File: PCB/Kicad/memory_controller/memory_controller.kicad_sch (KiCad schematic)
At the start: 4 parts

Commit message: fix
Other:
- removed sheet memory_tri_state_buffer
- sheet RegAddr ports: added ~{CLK_en}; removed nCLKen
- sheet input_MUX ports: added ~{OE}_n, ~{OE}_p; removed nOE_n, nOE_p
- sheet input_tri_state_buffer ports: added ~{OE}; removed nOE
- sheet memory_logic ports: added ~{OE}_MUX_n, ~{OE}_MUX_p, ~{WE}_mem; removed memory_logic_OUT, muxnOE_n, muxnOE_p, nWE_mem
- sheet mode_logic ports: added ~{OE}_n, ~{OE}_p, ~{OUTPUT_ENABLE}; removed nOE_n, nOE_p, nOUTPUT_ENABLE
- sheet output_MUX ports: added ~{OE}_n, ~{OE}_p; removed nOE_n, nOE_p
- sheet output_tri_state_buffer ports: added ~{OE}; removed nOE

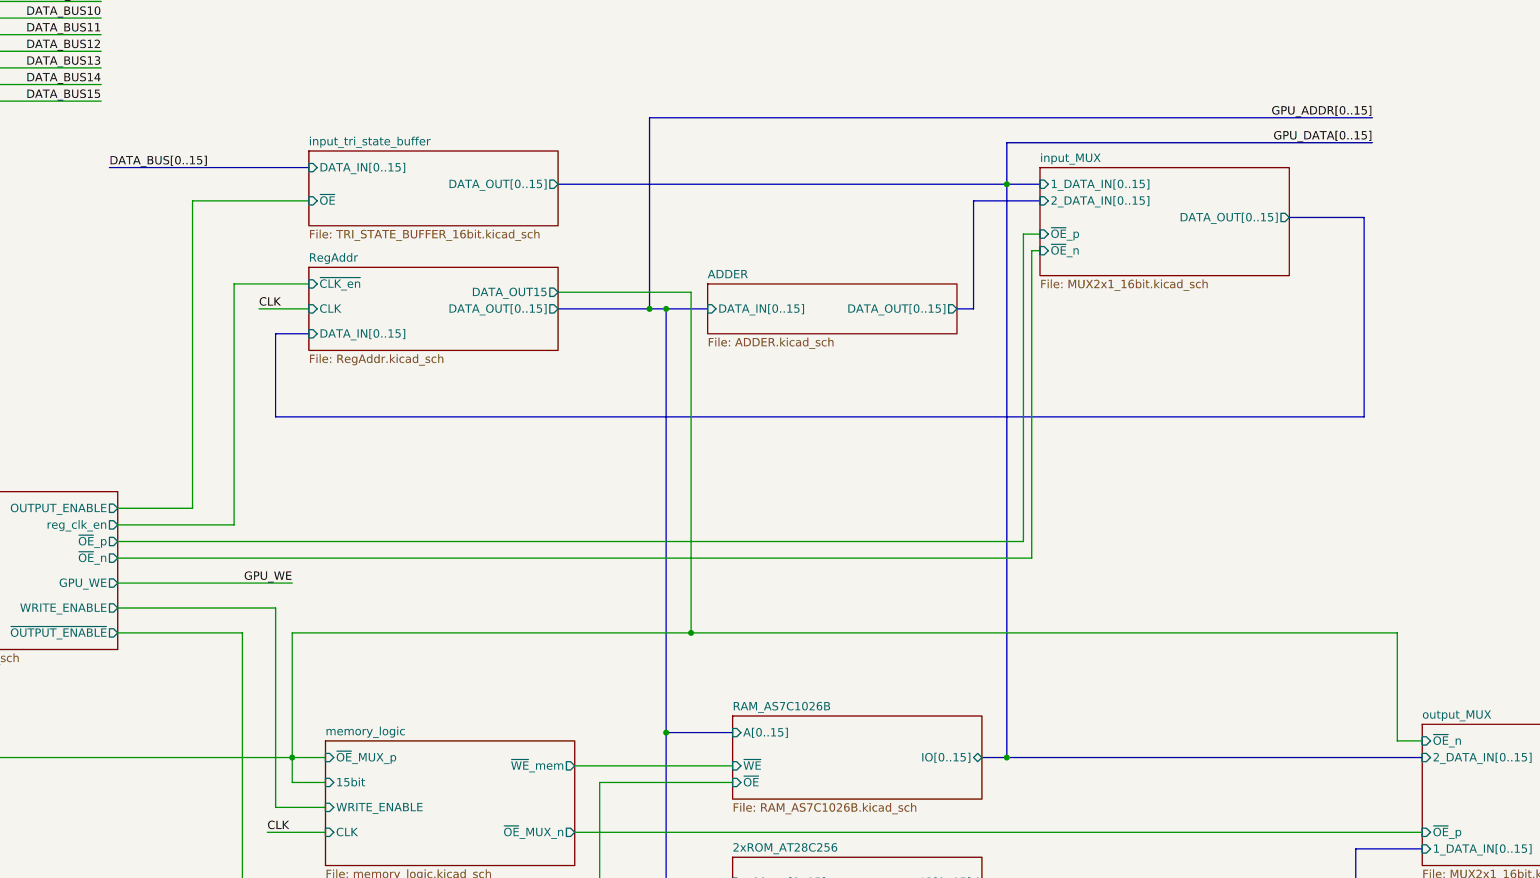
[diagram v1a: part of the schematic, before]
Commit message: memory controler fix
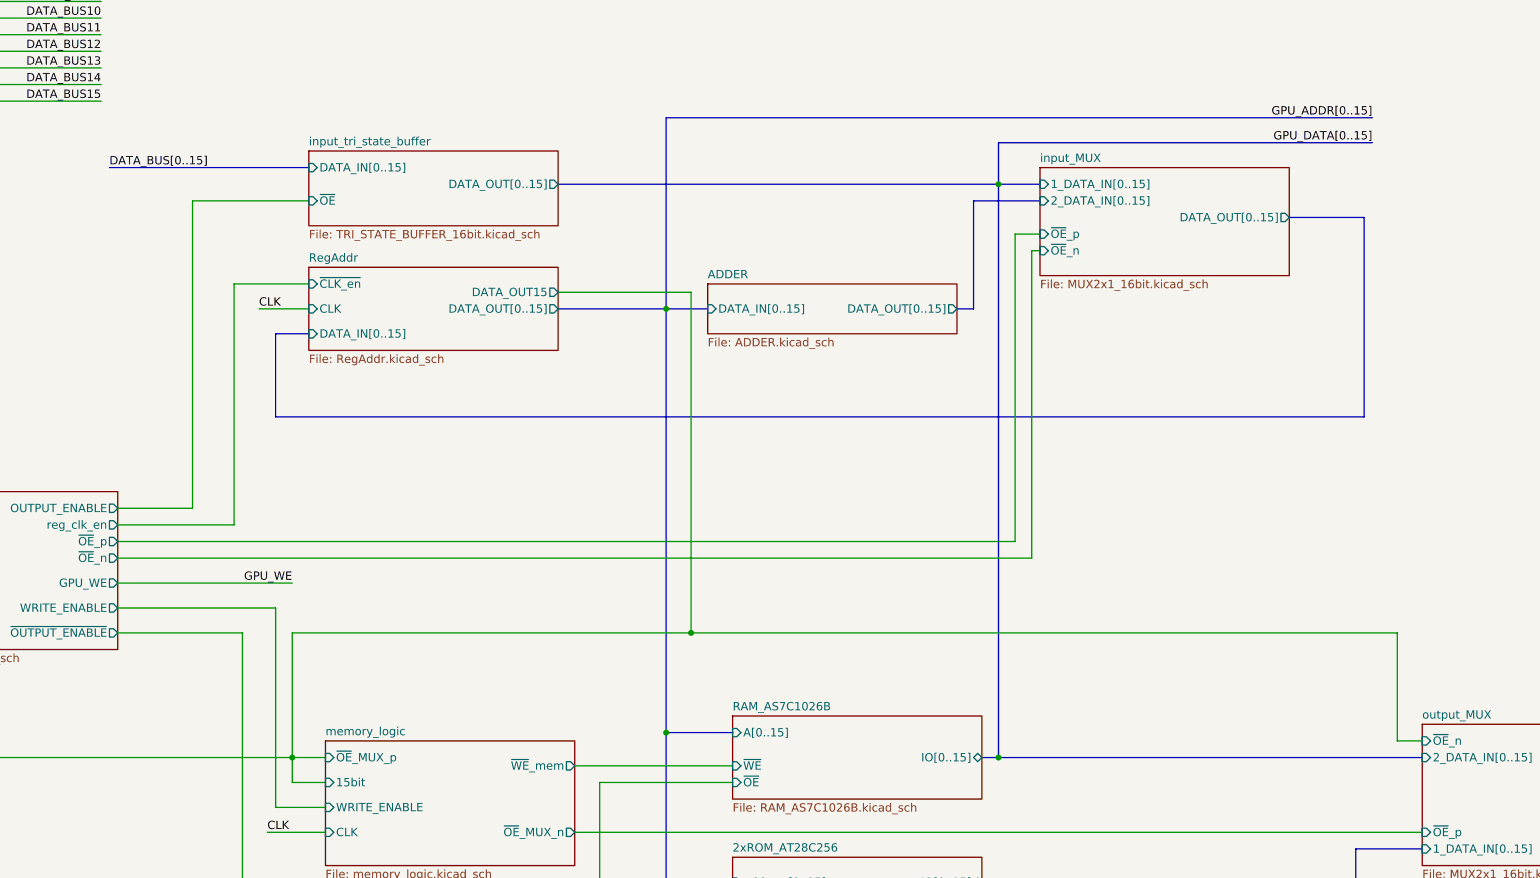
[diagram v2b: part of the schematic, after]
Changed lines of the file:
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@@
 	)
 	(junction
-		(at 227.33 191.77)
+		(at 226.06 191.77)
 		(diameter 0)
 		(color 0 0 0 0)
 	)
 	(junction
-		(at 227.33 104.14)
+		(at 226.06 104.14)
 		(diameter 0)
 		(color 0 0 0 0)
@@
 		(color 0 0 0 0)
 	)
-	(junction
-		(at 172.72 123.19)
-		(diameter 0)
-		(color 0 0 0 0)
-	)
 	(no_connect
 		(at 125.73 63.5)
@@
 	(bus
 		(pts
-			(xy 227.33 97.79) (xy 283.21 97.79)
+			(xy 226.06 97.79) (xy 283.21 97.79)
 		)
 		(stroke
@@
 	(bus
 		(pts
-			(xy 172.72 93.98) (xy 283.21 93.98)
+			(xy 175.26 93.98) (xy 283.21 93.98)
 		)
 		(stroke
@@
 	(bus
 		(pts
-			(xy 158.75 104.14) (xy 227.33 104.14)
+			(xy 158.75 104.14) (xy 226.06 104.14)
 		)
 		(stroke
@@
 	(bus
 		(pts
-			(xy 158.75 123.19) (xy 172.72 123.19)
+			(xy 158.75 123.19) (xy 175.26 123.19)
 		)
 		(stroke
@@
 	(bus
 		(pts
-			(xy 172.72 123.19) (xy 172.72 93.98)
+			(xy 175.26 123.19) (xy 175.26 93.98)
 		)
 		(stroke
@@
 		)
 	)
-	(bus
-		(pts
-			(xy 290.83 191.77) (xy 227.33 191.77)
-		)
-		(stroke
-			(width 0)
-			(type default)
-		)
-	)
 	(wire
 		(pts
@@
 	(wire
 		(pts
-			(xy 91.44 158.75) (xy 229.87 158.75)
+			(xy 91.44 158.75) (xy 228.6 158.75)
 		)
 		(stroke
@@
 	(wire
 		(pts
-			(xy 229.87 111.76) (xy 229.87 158.75)
+			(xy 228.6 111.76) (xy 228.6 158.75)
 		)
 		(stroke
@@
 	(bus
 		(pts
-			(xy 227.33 97.79) (xy 227.33 104.14)
+			(xy 226.06 97.79) (xy 226.06 104.14)
 		)
 		(stroke
@@
 		)
 	)
-	(bus
-		(pts
-			(xy 227.33 104.14) (xy 232.41 104.14)
-		)
-		(stroke
-			(width 0)
-			(type default)
-		)
-	)
 	(wire
 		(pts
@@
 		)
 	)
+	(bus
+		(pts
+			(xy 226.06 104.14) (xy 232.41 104.14)
+		)
+		(stroke
+			(width 0)
+			(type default)
+		)
+	)
 	(wire
 		(pts
@@
 		)
 	)
-	(bus
-		(pts
-			(xy 175.26 123.19) (xy 172.72 123.19)
-		)
-		(stroke
-			(width 0)
-			(type default)
-		)
-	)
 	(wire
 		(pts
@@
 	(bus
 		(pts
-			(xy 227.33 104.14) (xy 227.33 191.77)
+			(xy 226.06 104.14) (xy 226.06 191.77)
 		)
 		(stroke
@@
 	(wire
 		(pts
-			(xy 229.87 111.76) (xy 232.41 111.76)
+			(xy 228.6 111.76) (xy 232.41 111.76)
 		)
 		(stroke
@@
 		)
 	)
+	(bus
+		(pts
+			(xy 226.06 191.77) (xy 290.83 191.77)
+		)
+		(stroke
+			(width 0)
+			(type default)
+		)
+	)
 	(wire
 		(pts
@@
 	(bus
 		(pts
-			(xy 223.52 191.77) (xy 227.33 191.77)
-		)
-		(stroke
+			(xy 223.52 191.77) (xy 226.06 191.77)
+		)
+		(stroke

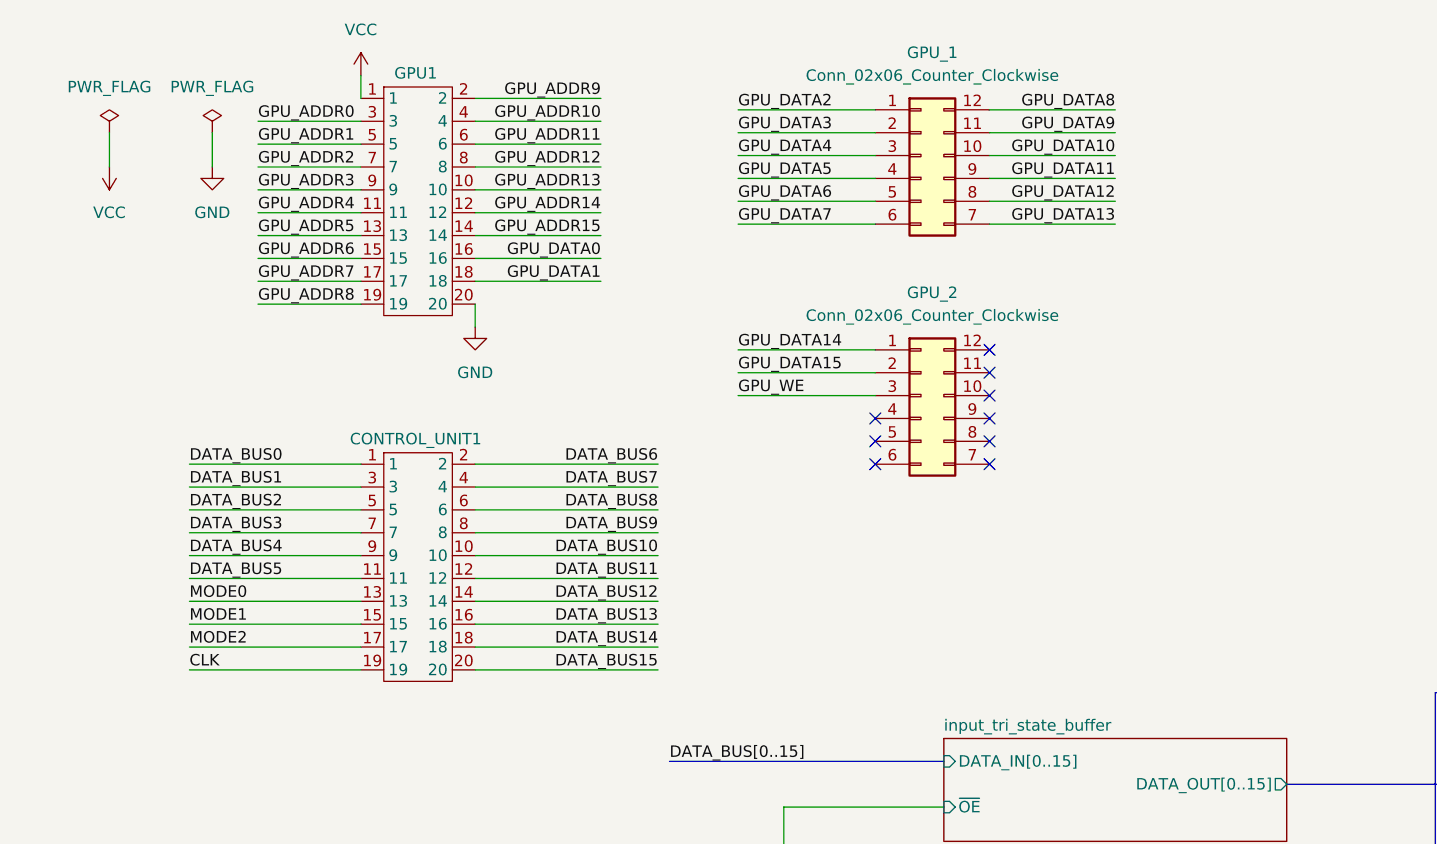
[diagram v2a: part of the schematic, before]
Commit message: kicad fix
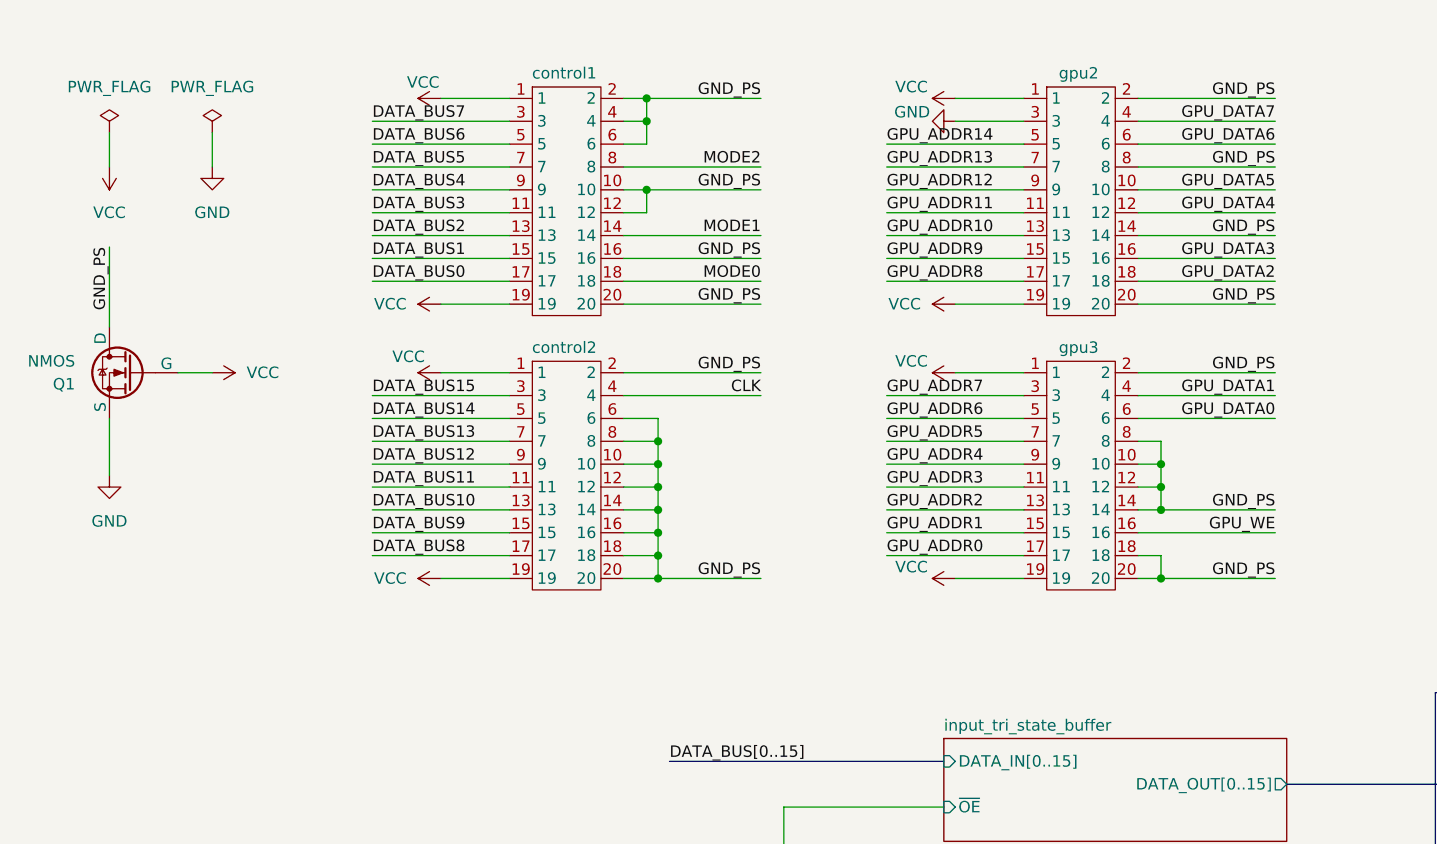
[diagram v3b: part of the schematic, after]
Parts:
- removed CONTROL_UNIT1, GPU1: ~, mALUch_lib:PinHeader_2x10_P2.54mm_Horizontal, symbol mALUch_lib:2x20_2.54_Horizontal
- removed GPU_1, GPU_2: Conn_02x06_Counter_Clockwise, symbol Connector_Generic:Conn_02x06_Counter_Clockwise
- added Q1: NMOS, symbol Simulation_SPICE:NMOS
- added control1, control2, gpu2, gpu3: ~, mALUch_lib:PinHeader_2x10_P2.54mm_Horizontal, symbol mALUch_lib:2x20_2.54_Horizontal
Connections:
- net CLK: now also control2.4
- net DATA_BUS0: now also control1.17
- net DATA_BUS1: now also control1.15
- net DATA_BUS10: now also control2.13
- net DATA_BUS11: now also control2.11
- net DATA_BUS12: now also control2.9
- net DATA_BUS13: now also control2.7
- net DATA_BUS14: now also control2.5
- net DATA_BUS15: now also control2.3
- net DATA_BUS2: now also control1.13
- net DATA_BUS3: now also control1.11
- net DATA_BUS4: now also control1.9
- net DATA_BUS5: now also control1.7
- net DATA_BUS6: now also control1.5
- net DATA_BUS7: now also control1.3
- net DATA_BUS8: now also control2.17
- net DATA_BUS9: now also control2.15
- net GND: now also Q1.3 (S), gpu2.3
- net GPU_ADDR0: now also gpu3.17
- net GPU_ADDR1: now also gpu3.15
- net GPU_ADDR10: now also gpu2.13
- net GPU_ADDR11: now also gpu2.11
- net GPU_ADDR12: now also gpu2.9
- net GPU_ADDR13: now also gpu2.7
- net GPU_ADDR14: now also gpu2.5
- net GPU_ADDR2: now also gpu3.13
- net GPU_ADDR3: now also gpu3.11
- net GPU_ADDR4: now also gpu3.9
- net GPU_ADDR5: now also gpu3.7
- net GPU_ADDR6: now also gpu3.5
- net GPU_ADDR7: now also gpu3.3
- net GPU_ADDR8: now also gpu2.17
- net GPU_ADDR9: now also gpu2.15
- net GPU_DATA0: now also gpu3.6
- net GPU_DATA1: now also gpu3.4
- net GPU_DATA2: now also gpu2.18
- net GPU_DATA3: now also gpu2.16
- net GPU_DATA4: now also gpu2.12
- net GPU_DATA5: now also gpu2.10
- net GPU_DATA6: now also gpu2.6
- net GPU_DATA7: now also gpu2.4
- net GPU_WE: now also gpu3.16
- net MODE0: now also control1.18
- net MODE1: now also control1.14
- net MODE2: now also control1.8
- net VCC: now also Q1.2 (G), control1.1, control1.19, control2.1, control2.19, gpu2.1, gpu2.19, gpu3.1, gpu3.19
- new net GND_PS: Q1.1 (D), control1.10, control1.12, control1.16, control1.2, control1.20, control1.4, control1.6, control2.10, control2.12, control2.14, control2.16, control2.18, control2.2, control2.20, control2.6, control2.8, gpu2.14, gpu2.2, gpu2.20, gpu2.8, gpu3.10, gpu3.12, gpu3.14, gpu3.18, gpu3.2, gpu3.20, gpu3.8
- no-connect marks 9 -> 0

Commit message: kicad memory controler
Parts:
- renumbered gpu2 to gpu1, gpu3 to gpu2
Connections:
- net GND: no longer gpu1.3
- net GND_PS: now also gpu1.3
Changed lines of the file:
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@@
 	(wire
 		(pts
+			(xy 114.3 30.48) (xy 129.54 30.48)
+		)
+		(stroke
+			(width 0)
+			(type default)
+		)
+	)
+	(wire
+		(pts
 			(xy 114.3 40.64) (xy 129.54 40.64)
 		)
@@
 	(wire
 		(pts
-			(xy 129.54 30.48) (xy 121.92 30.48)
-		)
-		(stroke
-			(width 0)
-			(type default)
-		)
-	)
-	(wire
-		(pts
 			(xy 49.53 191.77) (xy 118.11 191.77)
 		)
@@
 		)
 	)
+	(label "GND_PS"
+		(at 114.3 30.48 0)
+		(effects
+			(font
+				(size 1.27 1.27)
+			)
+			(justify left bottom)
+		)
+	)
 	(label "GPU_ADDR11"
 		(at 114.3 40.64 0)
@@
 	)
 	(symbol
-		(lib_id "power:GND")
-		(at 121.92 30.48 270)
-		(unit 1)
-		(exclude_from_sim no)
-		(in_bom yes)
-		(on_board yes)
-		(dnp no)
-		(property "Reference" "#PWR0142"
-			(at 115.57 30.48 0)
-			(effects
-				(font
-					(size 1.27 1.27)
-				)
-				(hide yes)
-			)
-		)
-		(property "Value" "GND"
-			(at 119.126 29.464 90)
-			(effects
-				(font
-					(size 1.27 1.27)
-				)
-				(justify right)
-			)
-		)
-		(property "Footprint" ""
-			(at 121.92 30.48 0)
-			(effects
-				(font
-					(size 1.27 1.27)
-				)
-				(hide yes)
-			)
-		)
-		(property "Datasheet" ""
-			(at 121.92 30.48 0)
-			(effects
-				(font
-					(size 1.27 1.27)
-				)
-				(hide yes)
-			)
-		)
-		(property "Description" "Power symbol creates a global label with name \"GND\" , ground"
-			(at 121.92 30.48 0)
-			(effects
-				(font
-					(size 1.27 1.27)
-				)
-				(hide yes)
-			)
-		)
-		(pin "1"
-		)
-		(instances
-			(project "memory_controller"
-				(path "/dccec861-b967-466c-843e-d6d1ad6064ce"
-					(reference "#PWR0142")
-					(unit 1)
-				)
-			)
-		)
-	)
-	(symbol
 		(lib_id "mALUch_lib:2x20_2.54_Horizontal")
 		(at 78.74 52.07 0)
@@
 		(on_board yes)
 		(dnp no)
-		(property "Reference" "gpu2"
+		(property "Reference" "gpu1"
 			(at 135.636 25.146 0)
 			(effects
@@
 			(project "memory_controller"
 				(path "/dccec861-b967-466c-843e-d6d1ad6064ce"
-					(reference "gpu2")
+					(reference "gpu1")
 					(unit 1)
 				)
@@
 		(on_board yes)
 		(dnp no)
-		(property "Reference" "gpu3"
+		(property "Reference" "gpu2"
 			(at 135.636 55.626 0)
 			(effects
@@
 			(project "memory_controller"
 				(path "/dccec861-b967-466c-843e-d6d1ad6064ce"
-					(reference "gpu3")
+					(reference "gpu2")
 					(unit 1)
 				)

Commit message: pcb init
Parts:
- removed Q1: NMOS, symbol Simulation_SPICE:NMOS
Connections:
- net GND_PS is gone; now on net GND: control1.10, control1.12, control1.16, control1.2, control1.20, control1.4, control1.6, control2.10, control2.12, control2.14, control2.16, control2.18, control2.2, control2.20, control2.6, control2.8, gpu1.14, gpu1.2, gpu1.20, gpu1.3, gpu1.8, gpu2.10, gpu2.12, gpu2.14, gpu2.18, gpu2.2, gpu2.20, gpu2.8

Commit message: LEDs + minor fixes
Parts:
- added Dd1, Dd10, Dd11, Dd12, Dd2, Dd3, Dd4, Dd5, Dd6, Dd7, Dd8, Dd9: yellow, LED_SMD:LED_0603_1608Metric, symbol Device:LED
- added Dpwr1: green, Diode_SMD:D_0603_1608Metric, symbol Device:LED
- added H1, H2, H3, H4: MountingHole_Pad, MountingHole:MountingHole_2.2mm_M2_DIN965_Pad, symbol Mechanical:MountingHole_Pad
- added Rd1, Rd10, Rd11, Rd12, Rd2, Rd3, Rd4, Rd5, Rd6, Rd7, Rd8, Rd9, Rgp1: 680, Resistor_SMD:R_0402_1005Metric, symbol Device:R
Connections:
- net GND: now also H1.1, H2.1, H3.1, H4.1, Rd1.2, Rd10.2, Rd11.2, Rd12.2, Rd2.2, Rd3.2, Rd4.2, Rd5.2, Rd6.2, Rd7.2, Rd8.2, Rd9.2, Rgp1.2
- net GPU_WE: now also Dd4.2 (A)
- net MODE1: now also Dd11.2 (A)
- net MODE2: now also Dd12.2 (A)
- net RegAddr/DATA_OUT15: now also Dd9.2 (A)
- net VCC: now also Dpwr1.2 (A)
- net MODE0 renamed ~{OE}_n
- net ~{OE}_n: now also Dd10.2 (A), Dd2.2 (A)
- new net: Dd8.1 (K), Rd8.1
- new net: Dd12.1 (K), Rd12.1
- new net: Dd6.1 (K), Rd6.1
- new net: Dd5.1 (K), Rd5.1
- new net: Dd9.1 (K), Rd9.1
- new net: Dd10.1 (K), Rd10.1
- new net: Dd1.1 (K), Rd1.1
- new net: Dd11.1 (K), Rd11.1
- new net: Dpwr1.1 (K), Rgp1.1
- new net: Dd3.1 (K), Rd3.1
- new net: Dd4.1 (K), Rd4.1
- new net: Dd2.1 (K), Rd2.1
- new net: Dd7.1 (K), Rd7.1
- new net OUTPUT_ENABLE: Dd3.2 (A)
- new net WRITE_ENABLE: Dd8.2 (A)
- new net ~{OE}_MUX_n: Dd6.2 (A)
- new net ~{OE}_p: Dd1.2 (A)
- new net ~{OUTPUT_ENABLE}: Dd7.2 (A)
- new net ~{WE}_mem: Dd5.2 (A)
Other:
- note added: "DATA_OUT15"
- note added: "MODE0"
- note added: "MODE_0"
- note added: "POWER LED"

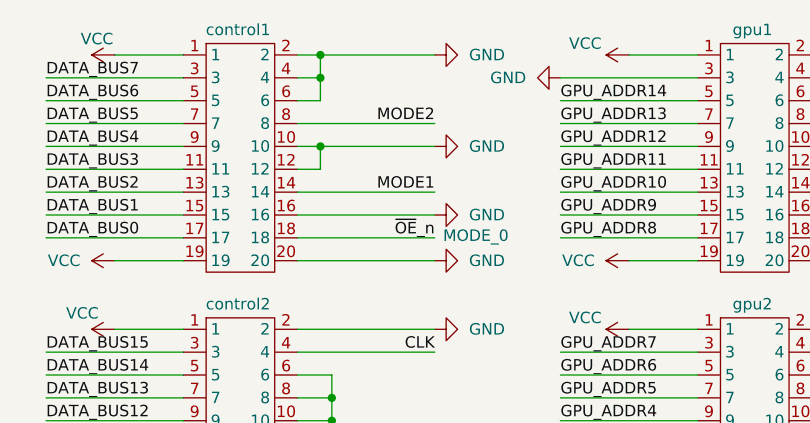
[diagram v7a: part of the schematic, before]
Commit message: memory controller schematic update
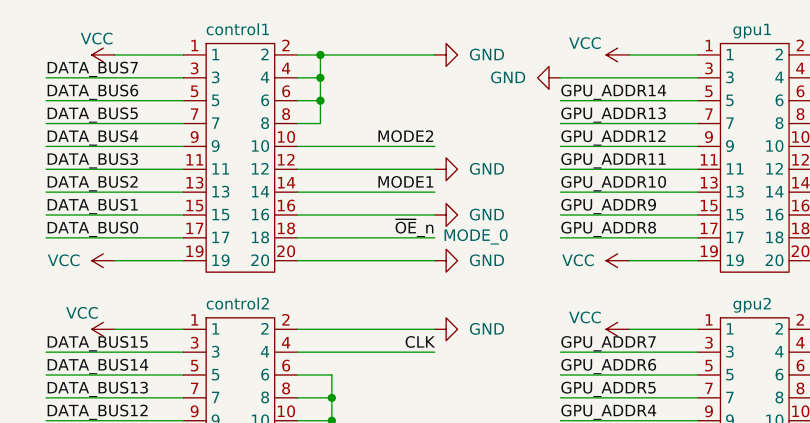
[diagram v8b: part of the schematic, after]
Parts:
- Dpwr1: footprint Diode_SMD:D_0603_1608Metric -> LED_SMD:LED_0603_1608Metric
- control1, control2: value ~ -> out
- gpu1, gpu2: value ~ -> in
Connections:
- net GND: now also control1.8; no longer control1.10
- net MODE2: now also control1.10; no longer control1.8
